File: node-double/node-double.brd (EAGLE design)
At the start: 35.1 x 24.3 mm, 33 parts, among them IC1 TP4056, IC3 24C02, U1 ATMEGA328P_TQFP, U2 3.3V/150mA

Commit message: Node: Adding interrupt pin
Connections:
- removed net IRQ: U$1.IRQ
- net D2: now also U$1.IRQ
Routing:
- net D2: track 0.00 -> 13.0 mm, vias 0 -> 1
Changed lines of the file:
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@@
 <contactref element="R3" pad="2"/>
 <contactref element="R2" pad="2"/>
+<wire x1="23.9395" y1="27.217" x2="22.6695" y2="27.0265" width="0" layer="19" extent="1-16"/>
+<wire x1="32.004" y1="26.0385" x2="32.6865" y2="23.6855" width="0" layer="19" extent="1-1"/>
 </signal>
 <signal name="VCC">
@@
 <signal name="D2">
 <contactref element="U1" pad="32"/>
+<contactref element="U$1" pad="IRQ"/>
+<wire x1="24.5745" y1="37.719" x2="25.5905" y2="37.719" width="0.1524" layer="16"/>
+<wire x1="25.5905" y1="37.719" x2="25.732925" y2="37.576575" width="0.1524" layer="16"/>
+<via x="25.732925" y="37.576575" extent="1-16" drill="0.35"/>
+<wire x1="25.9997" y1="34.61015" x2="26.35515" y2="34.2547" width="0.1524" layer="1"/>
+<wire x1="26.35515" y1="34.2547" x2="26.85785" y2="34.2547" width="0.1524" layer="1"/>
+<wire x1="29.2989" y1="33.244675" x2="29.879175" y2="32.6644" width="0.1524" layer="1"/>
+<wire x1="29.879175" y1="32.6644" x2="30.699825" y2="32.6644" width="0.1524" layer="1"/>
+<wire x1="31.430425" y1="33.395" x2="32.5374" y2="33.395" width="0.1524" layer="1"/>
+<wire x1="30.699825" y1="32.6644" x2="31.430425" y2="33.395" width="0.1524" layer="1"/>
+<wire x1="25.732925" y1="37.576575" x2="25.9997" y2="37.3098" width="0.1524" layer="1"/>
+<wire x1="25.9997" y1="37.3098" x2="25.9997" y2="34.61015" width="0.1524" layer="1"/>
+<wire x1="26.85785" y1="34.2547" x2="27.44826875" y2="34.904421875" width="0.1524" layer="1"/>
+<wire x1="27.44826875" y1="34.904421875" x2="27.49005" y2="34.9504" width="0.1524" layer="1"/>
+<wire x1="29.2989" y1="33.84005" x2="29.2989" y2="33.244675" width="0.1524" layer="1"/>
+<wire x1="27.44826875" y1="34.904421875" x2="27.532346875" y2="34.9885" width="0.1524" layer="1"/>
+<wire x1="28.15045" y1="34.9885" x2="29.2989" y2="33.84005" width="0.1524" layer="1"/>
+<wire x1="27.532346875" y1="34.9885" x2="28.15045" y2="34.9885" width="0.1524" layer="1"/>
 </signal>
 <signal name="D3">
@@
 <wire x1="46.438" y1="35.218" x2="46.78" y2="35.56" width="0.1524" layer="1"/>
 </signal>
-<signal name="IRQ">
-<contactref element="U$1" pad="IRQ"/>
-</signal>
 <signal name="N$1">

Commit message: Node Double v0.6
- Rounded PCB Corner
- Switched to Tented Vias
- Large M3 Mounting Hole
- LEDs slightly distant from the RF module pins
- Cutout copper from beneath the RF antenna
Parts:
- moved LED1 0.51 mm to (22.2, 31.1)
- moved LED2 0.51 mm to (22.2, 38.4)
- moved R2 0.51 mm to (22.2, 27.9)
- moved R3 0.51 mm to (22.2, 35.1)
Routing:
- net GND: track 5.22 -> 25.4 mm, vias 4 -> 5
- net D2: track 13.0 -> 13.7 mm
- added copper zone on layer 16, net N$3
- added copper zone on layer 16, net N$4
- added copper zone on layer 1, net N$5
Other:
- outline, holes or cut-outs redrawn
- board text added: "v0.6 Beta"
- board text removed: "v0.4 Beta"

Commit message: Scratch progress
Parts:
- removed C4: 10u, resistor:C0603
- removed IC3: 24C02, microchip:SO-08
- C1, C2, C3, C5, C7, C9: device resistor:C0603 -> Nordic_nRF:RESC0603_L
- C6: value 0.1u -> 100n; device resistor:C0603 -> Nordic_nRF:RESC0603_L
- R1, R14, R15, R2, R3, R4, R5, R6: device resistor:R0603 -> SparkFun-Resistors:0603
- R10, R11: value 100k -> 100K; device resistor:R0603 -> SparkFun-Resistors:0603
- R12, R8: value 470k -> 470K; device resistor:R0603 -> SparkFun-Resistors:0603
- moved C2 10.2 mm to (39.4, 24.3), turned to 270 degrees
- moved IC1 9.55 mm to (43.7, 27.4)
- moved C3 9.40 mm to (46.4, 23.5)
- moved R8 9.04 mm to (46.6, 31.0), turned to 180 degrees
- moved U$1 7.75 mm to (30.2, 33.7)
- moved R10 7.73 mm to (46.6, 32.4), turned to 180 degrees
- moved R11 7.66 mm to (46.6, 35.4), turned to 180 degrees
- moved U2 7.43 mm to (52.6, 26.5), turned to 270 degrees
- moved C10 7.31 mm to (29.6, 32.7)
- moved R12 7.22 mm to (46.6, 33.9), turned to 180 degrees
- moved R6 6.10 mm to (42.5, 30.4), turned to 0 degrees
- moved C8 5.79 mm to (29.6, 32.6), flipped to the bottom
- moved R4 5.38 mm to (48.9, 28.7), turned to 0 degrees
- moved R14 4.94 mm to (28.6, 26.2)
- moved R15 4.88 mm to (30.7, 26.2)
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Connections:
- net D3: no longer IC3.7
- net D7: now also IC1.6, R5.1; no longer IC1.7, R4.1
- net D8: now also IC1.7, R4.1; no longer IC1.6, R5.1
- net GND: no longer C4.2, IC3.1, IC3.2, IC3.3, IC3.4
- net SCL/A5: no longer IC3.6
- net SDA/A4: no longer IC3.5
- net VBAT: no longer C4.1
- net VCC: no longer IC3.8
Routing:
- net VCC: track 87.3 -> 0.00 mm, vias 3 -> 0
- net VIN: track 31.7 -> 0.00 mm, vias 3 -> 0
- net D6: track 26.4 -> 0.00 mm, vias 1 -> 0
- net GND: track 25.4 -> 0.00 mm, vias 5 -> 0
- net SCK/13: track 25.3 -> 0.00 mm, vias 1 -> 0
- net SCL/A5: track 25.3 -> 0.00 mm
- net SDA/A4: track 25.0 -> 0.00 mm
- net VBAT: track 23.9 -> 0.00 mm
- net D7: track 22.8 -> 0.00 mm, vias 3 -> 0
- net D8: track 22.4 -> 0.00 mm, vias 3 -> 0
- net D9: track 22.0 -> 0.00 mm, vias 1 -> 0
- net MISO/12: track 21.2 -> 0.00 mm, vias 1 -> 0
- net A7: track 20.0 -> 0.00 mm, vias 2 -> 0
- net MOSI/11: track 19.8 -> 0.00 mm, vias 1 -> 0
- net D10: track 19.0 -> 0.00 mm, vias 1 -> 0
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- added copper zone on layer 16, net VCC
- removed copper zone on layer 16, net GND
- removed copper zone on layer 16, net N$3
- removed copper zone on layer 16, net N$4
- removed copper zone on layer 1, net N$5
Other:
- outline, holes or cut-outs redrawn

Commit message: Routing & VCC Optimization
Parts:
- moved C1 0.20 mm to (36.3, 42.5)
- moved R1 0.06 mm to (33.6, 42.3)
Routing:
- net GND: track 0.00 -> 52.7 mm, vias 0 -> 11
- net SDA/A4: track 0.00 -> 44.3 mm, vias 0 -> 2
- net D6: track 0.00 -> 36.6 mm, vias 0 -> 1
- net VCC: track 0.00 -> 30.1 mm, vias 0 -> 9
- net D4: track 0.00 -> 27.3 mm, vias 0 -> 1
- net VBAT: track 0.00 -> 24.3 mm, vias 0 -> 1
- net SCK/13: track 0.00 -> 24.0 mm, vias 0 -> 2
- net MISO/12: track 0.00 -> 22.7 mm, vias 0 -> 1
- net MOSI/11: track 0.00 -> 20.1 mm, vias 0 -> 2
- net VIN: track 0.00 -> 19.9 mm
- net SCL/A5: track 0.00 -> 17.2 mm
- net A7: track 0.00 -> 14.8 mm
- net D2: track 0.00 -> 13.7 mm, vias 0 -> 1
- net A6: track 0.00 -> 13.3 mm, vias 0 -> 2
- net D9: track 0.00 -> 13.0 mm, vias 0 -> 1
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
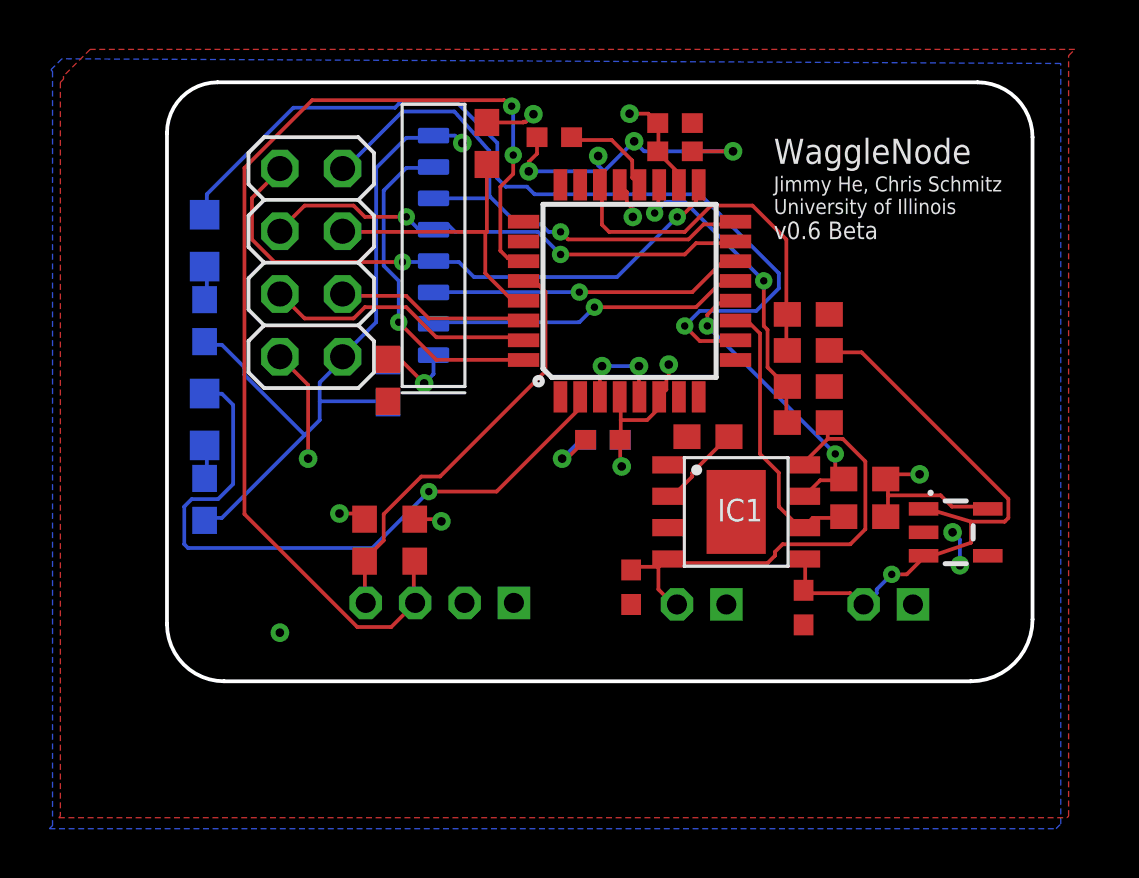
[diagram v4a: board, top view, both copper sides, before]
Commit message: Routing massively cleaned up
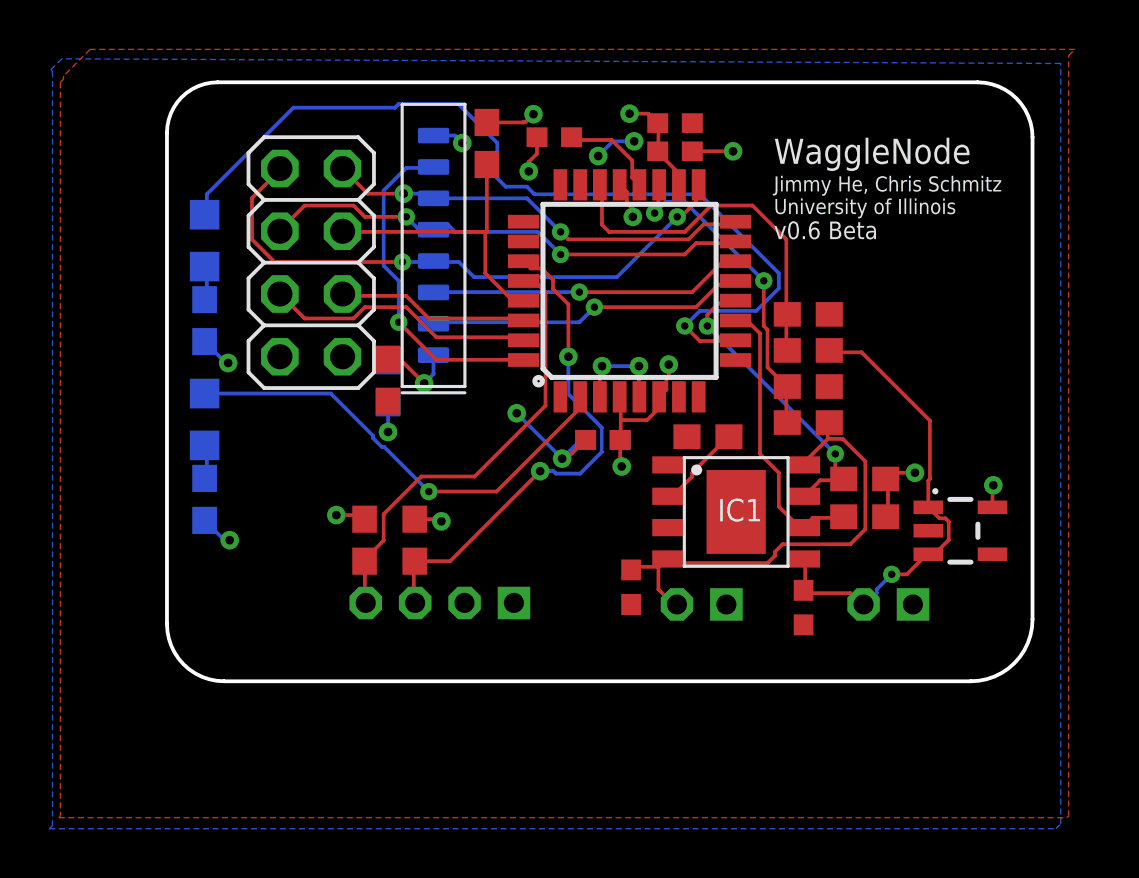
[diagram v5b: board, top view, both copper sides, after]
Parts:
- moved U2 0.20 mm to (52.8, 26.6)
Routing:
- net GND: track 52.7 -> 20.7 mm, vias 11 -> 13
- net SDA/A4: track 44.3 -> 20.5 mm
- net D4: track 27.3 -> 18.8 mm
- net VCC: track 30.1 -> 22.0 mm
- net MISO/12: track 22.7 -> 17.4 mm, vias 1 -> 2
- net VBAT: track 24.3 -> 19.3 mm
- net SCL/A5: track 17.2 -> 18.0 mm

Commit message: Node 0.8: Pour cutout for radio antenna
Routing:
- net VBAT: track 19.3 -> 20.2 mm
- net GND: track 20.7 -> 21.3 mm
- added copper zone on layer 16, net GND
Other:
- board text added: "v0.8 Beta"
- board text removed: "v0.6 Beta"
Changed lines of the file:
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@@
 <setting verticaltext="up"/>
 </settings>
-<grid distance="2.5" unitdist="mil" unit="mil" style="lines" multiple="1" display="no" altdistance="2.5" altunitdist="mil" altunit="mil"/>
+<grid distance="5" unitdist="mil" unit="mil" style="lines" multiple="1" display="no" altdistance="2.5" altunitdist="mil" altunit="mil"/>
 <layers>
 <layer number="1" name="Top" color="4" fill="1" visible="yes" active="yes"/>
@@
 <wire x1="22.68521875" y1="44.7675" x2="20.6375" y2="42.71978125" width="0.1524" layer="20" curve="90"/>
 <text x="45.212" y="41.4655" size="1.016" layer="21">WaggleNode</text>
-<text x="45.212" y="38.4175" size="0.7112" layer="21">v0.6 Beta</text>
+<text x="45.212" y="38.4175" size="0.7112" layer="21">v0.8 Beta</text>
 <text x="45.212" y="39.4335" size="0.6096" layer="21">Jimmy He, Chris Schmitz
 University of Illinois</text>
@@
 <contactref element="J_BATT" pad="1"/>
 <contactref element="U$1" pad="GND"/>
-<polygon width="0.1524" layer="1">
+<polygon width="0.1524" layer="1" isolate="0.1524">
 <vertex x="16.3195" y="44.7675"/>
 <vertex x="16.3195" y="15.0495"/>
@@
 <wire x1="22.9625" y1="26.2255" x2="23.1775" y2="26.2255" width="0.1524" layer="16"/>
 <via x="23.1775" y="26.2255" extent="1-16" drill="0.35"/>
+<polygon width="0.1524" layer="1" pour="cutout">
+<vertex x="46.99" y="45.72"/>
+<vertex x="46.99" y="33.02"/>
+<vertex x="57.15" y="33.02"/>
+<vertex x="57.15" y="45.72"/>
+</polygon>
+<polygon width="0.1524" layer="16" pour="cutout">
+<vertex x="46.99" y="45.72"/>
+<vertex x="46.99" y="33.02"/>
+<vertex x="57.15" y="33.02"/>
+<vertex x="57.15" y="45.72"/>
+</polygon>
+<wire x1="47.459" y1="35.3695" x2="46.7995" y2="35.3695" width="0.1524" layer="1"/>
 </signal>
 <signal name="VCC">
@@
 <contactref element="U$1" pad="VCC"/>
 <contactref element="U$2" pad="7"/>
-<polygon width="0.1524" layer="16">
+<polygon width="0.1524" layer="16" isolate="0.1524">
 <vertex x="16.002" y="45.212"/>
 <vertex x="16.002" y="14.6685"/>
@@
 <contactref element="J_BATT" pad="2"/>
 <contactref element="U2" pad="1"/>
-<wire x1="46.482" y1="25.4508" x2="46.482" y2="24.2316" width="0.1524" layer="1"/>
-<wire x1="46.482" y1="24.2316" x2="46.4185" y2="24.195" width="0.1524" layer="1"/>
-<wire x1="46.482" y1="25.4508" x2="46.438" y2="25.4635" width="0.1524" layer="1"/>
-<wire x1="48.3108" y1="24.0792" x2="46.482" y2="24.0792" width="0.1524" layer="1"/>
-<wire x1="48.768" y1="23.622" x2="48.3108" y2="24.0792" width="0.1524" layer="1"/>
-<wire x1="46.482" y1="24.0792" x2="46.4185" y2="24.195" width="0.1524" layer="1"/>
-<wire x1="48.768" y1="23.622" x2="48.8475" y2="23.622" width="0.1524" layer="1"/>
+<wire x1="46.482" y1="25.4508" x2="46.482" y2="24.2316" width="0.3048" layer="1"/>
+<wire x1="46.482" y1="24.2316" x2="46.4185" y2="24.195" width="0.3048" layer="1"/>
+<wire x1="46.482" y1="25.4508" x2="46.438" y2="25.4635" width="0.3048" layer="1"/>
+<wire x1="48.3108" y1="24.0792" x2="46.482" y2="24.0792" width="0.3048" layer="1"/>
+<wire x1="48.768" y1="23.622" x2="48.3108" y2="24.0792" width="0.3048" layer="1"/>
+<wire x1="46.482" y1="24.0792" x2="46.4185" y2="24.195" width="0.3048" layer="1"/>
+<wire x1="48.768" y1="23.622" x2="48.8475" y2="23.622" width="0.3048" layer="1"/>
 <wire x1="48.768" y1="33.8328" x2="47.5488" y2="33.8328" width="0.1524" layer="1"/>
-<wire x1="47.5488" y1="33.8328" x2="47.459" y2="33.909" width="0.1524" layer="1"/>
-<wire x1="51.6636" y1="25.6032" x2="51.501225" y2="25.623675" width="0.1524" layer="1"/>
-<wire x1="49.3776" y1="24.0792" x2="48.9204" y2="23.622" width="0.1524" layer="16"/>
-<wire x1="49.3776" y1="24.2316" x2="49.3776" y2="24.0792" width="0.1524" layer="16"/>
-<wire x1="49.9872" y1="24.8412" x2="49.3776" y2="24.2316" width="0.1524" layer="16"/>
-<wire x1="50.5968" y1="24.8412" x2="49.9872" y2="24.8412" width="0.1524" layer="1"/>
-<wire x1="51.3551625" y1="25.5995625" x2="50.5968" y2="24.8412" width="0.1524" layer="1"/>
-<wire x1="48.9204" y1="23.622" x2="48.8475" y2="23.622" width="0.1524" layer="16"/>
-<wire x1="51.3551625" y1="25.5995625" x2="51.4684" y2="25.6565" width="0.1524" layer="1"/>
+<wire x1="47.5488" y1="33.8328" x2="47.459" y2="33.909" width="0.3048" layer="1"/>
+<wire x1="52.0019375" y1="25.5605375" x2="51.501225" y2="25.623675" width="0.3048" layer="1"/>
+<wire x1="49.3776" y1="24.0792" x2="48.9204" y2="23.622" width="0.3048" layer="16"/>
+<wire x1="49.3776" y1="24.2316" x2="49.3776" y2="24.0792" width="0.3048" layer="16"/>
+<wire x1="49.9872" y1="24.8412" x2="49.3776" y2="24.2316" width="0.3048" layer="16"/>
+<wire x1="50.5968" y1="24.8412" x2="49.9872" y2="24.8412" width="0.3048" layer="1"/>
+<wire x1="51.3551625" y1="25.5995625" x2="50.5968" y2="24.8412" width="0.3048" layer="1"/>
+<wire x1="48.9204" y1="23.622" x2="48.8475" y2="23.622" width="0.3048" layer="16"/>
+<wire x1="51.3551625" y1="25.5995625" x2="51.4684" y2="25.6565" width="0.3048" layer="1"/>
 <via x="49.9872" y="24.8412" extent="1-16" drill="0.3"/>
-<wire x1="51.501225" y1="25.623675" x2="51.4684" y2="25.6565" width="0.1524" layer="1"/>
-<wire x1="52.1630875" y1="27.1101" x2="52.297" y2="26.9761875" width="0.1524" layer="1"/>
-<wire x1="52.297" y1="26.9761875" x2="52.297" y2="26.2368125" width="0.1524" layer="1"/>
-<wire x1="51.9148" y1="27.1101" x2="52.1630875" y2="27.1101" width="0.1524" layer="1"/>
-<wire x1="51.6636" y1="25.6034125" x2="51.6636" y2="25.6032" width="0.1524" layer="1"/>
-<wire x1="52.297" y1="26.2368125" x2="51.6636" y2="25.6034125" width="0.1524" layer="1"/>
-<wire x1="51.4684" y1="27.5565" x2="51.9148" y2="27.1101" width="0.1524" layer="1"/>
-<wire x1="51.5338" y1="28.70465" x2="51.4684" y2="28.63925" width="0.1524" layer="1"/>
-<wire x1="51.5338" y1="28.70465" x2="51.5338" y2="31.067" width="0.1524" layer="1"/>
-<wire x1="51.5338" y1="31.067" x2="48.768" y2="33.8328" width="0.1524" layer="1"/>
-<wire x1="51.4684" y1="28.63925" x2="51.4684" y2="27.5565" width="0.1524" layer="1"/>
+<wire x1="51.501225" y1="25.623675" x2="51.4684" y2="25.6565" width="0.3048" layer="1"/>
+<wire x1="51.8494" y1="27.5565" x2="52.551071875" y2="26.854828125" width="0.3048" layer="1"/>
+<wire x1="52.551071875" y1="26.854828125" x2="52.551071875" y2="26.109671875" width="0.3048" layer="1"/>
+<wire x1="52.551071875" y1="26.109671875" x2="52.0019375" y2="25.5605375" width="0.3048" layer="1"/>
+<wire x1="52.0418" y1="28.57765" x2="51.4684" y2="28.00425" width="0.1524" layer="1"/>
+<wire x1="52.0418" y1="28.57765" x2="52.0418" y2="30.559" width="0.1524" layer="1"/>
+<wire x1="52.0418" y1="30.559" x2="48.768" y2="33.8328" width="0.1524" layer="1"/>
+<wire x1="51.4684" y1="28.00425" x2="51.4684" y2="27.5565" width="0.1524" layer="1"/>
+<wire x1="51.4684" y1="27.5565" x2="51.8494" y2="27.5565" width="0.3048" layer="1"/>
 </signal>
 <signal name="VIN">
@@
 <mfgpreviewcolor name="substratecolor" color="0xFF786E46"/>
 </mfgpreviewcolors>
+<errors>
+</errors>
 </board>
 </drawing>

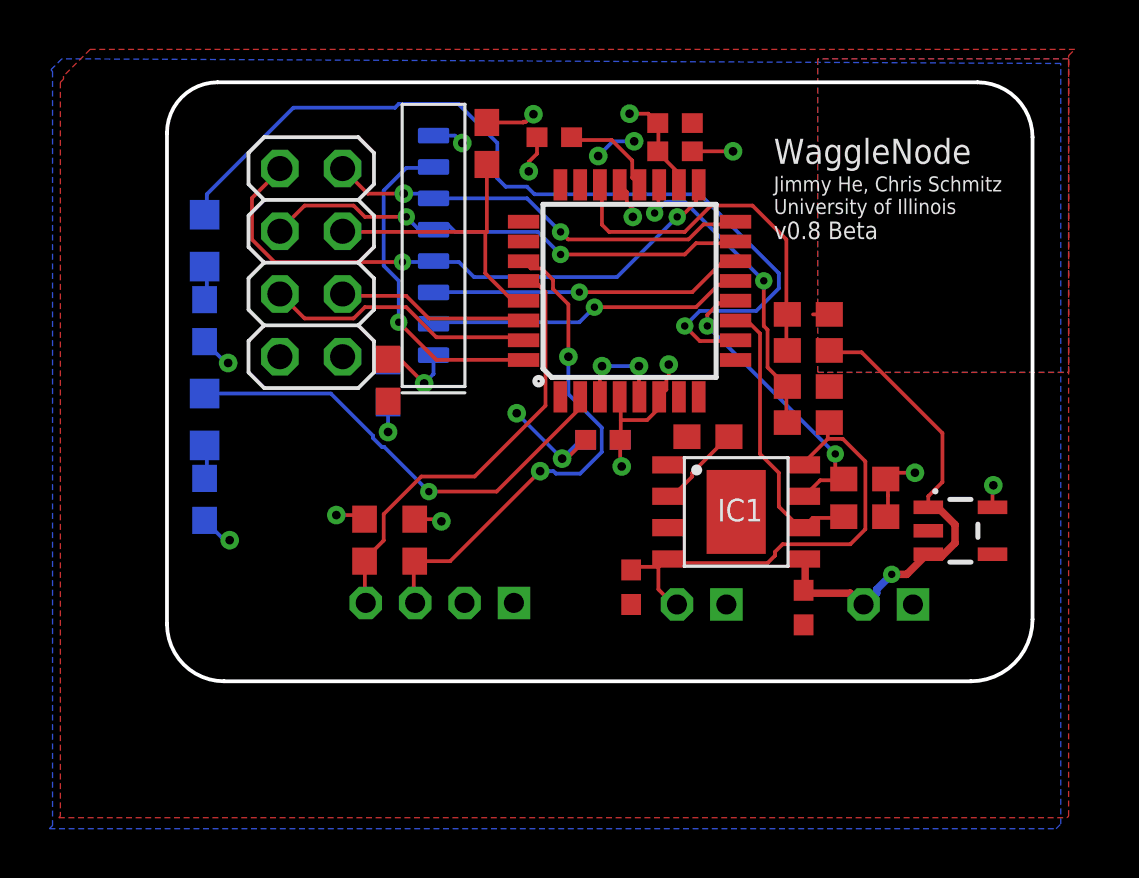
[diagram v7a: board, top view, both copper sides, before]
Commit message: Post-ramp circuit fixes
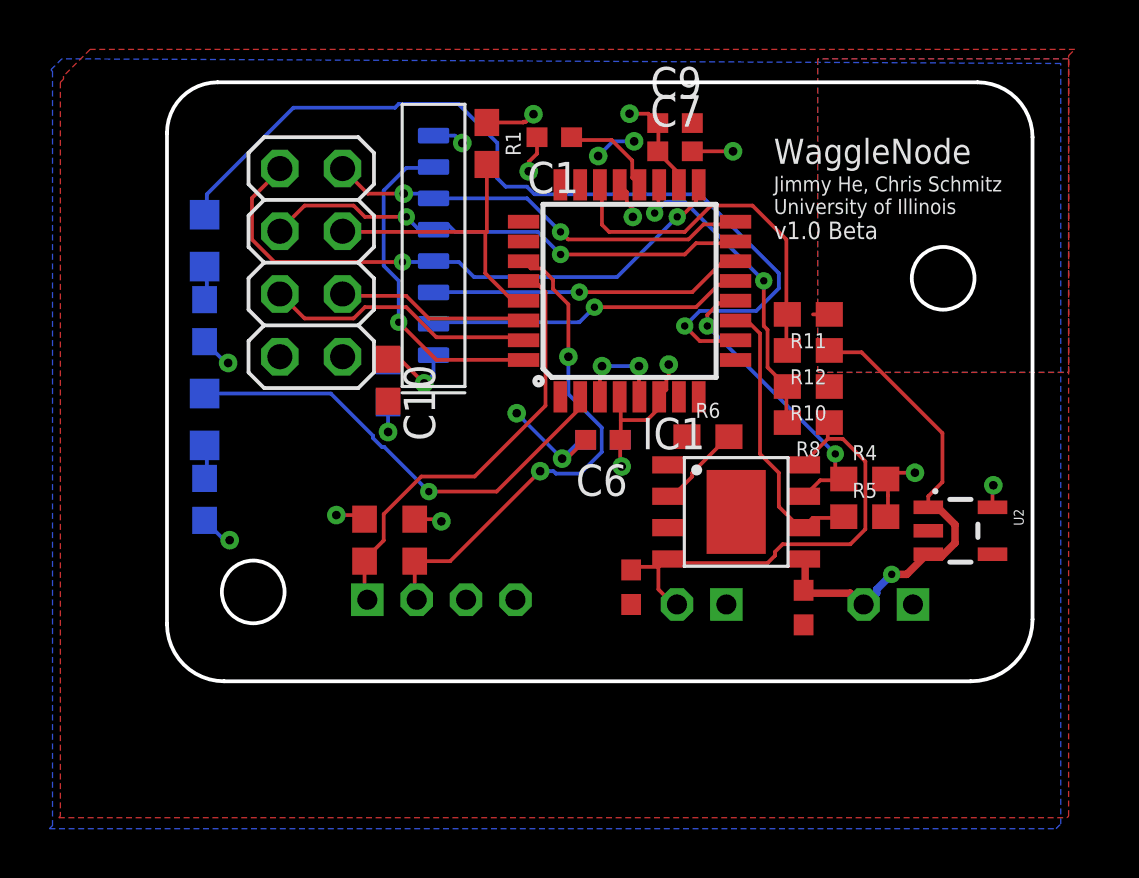
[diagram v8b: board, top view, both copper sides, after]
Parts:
- removed SENSOR: B4B-PH-K, con-jst-ph:B4B-PH-K
- added SENSOR1: B4B-PH-K, con-jst-ph:B4B-PH-K
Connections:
- net GND: now also SENSOR1.3; no longer SENSOR.2
- net SCL/A5: now also SENSOR1.1; no longer SENSOR.4
- net SDA/A4: now also SENSOR1.2; no longer SENSOR.3
- net VCC: now also SENSOR1.4; no longer SENSOR.1
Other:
- outline, holes or cut-outs redrawn
- board text added: "v1.0 Beta"
- board text removed: "v0.8 Beta"
